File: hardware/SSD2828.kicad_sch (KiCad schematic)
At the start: 61 parts, among them IC1 TLV62568DBVR, J1 FH35C-25S-0.3SHW_50_, J3 Conn_01x34, U1 PAM2306DYPAA, U2 SSD2828QN4, Y1 24mhz

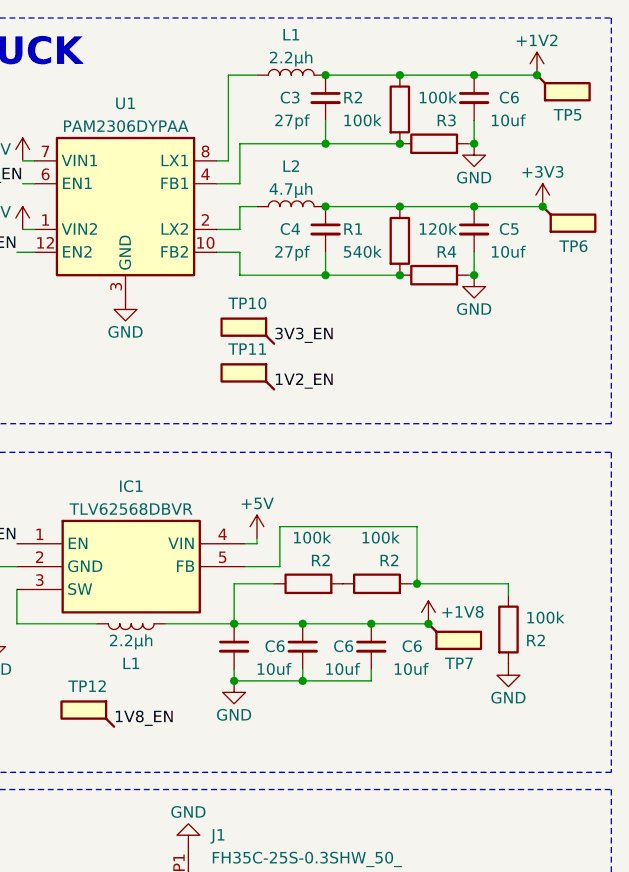
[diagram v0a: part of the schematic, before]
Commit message: added solder bridges on all the generated voltage rails on the SSD2828 board
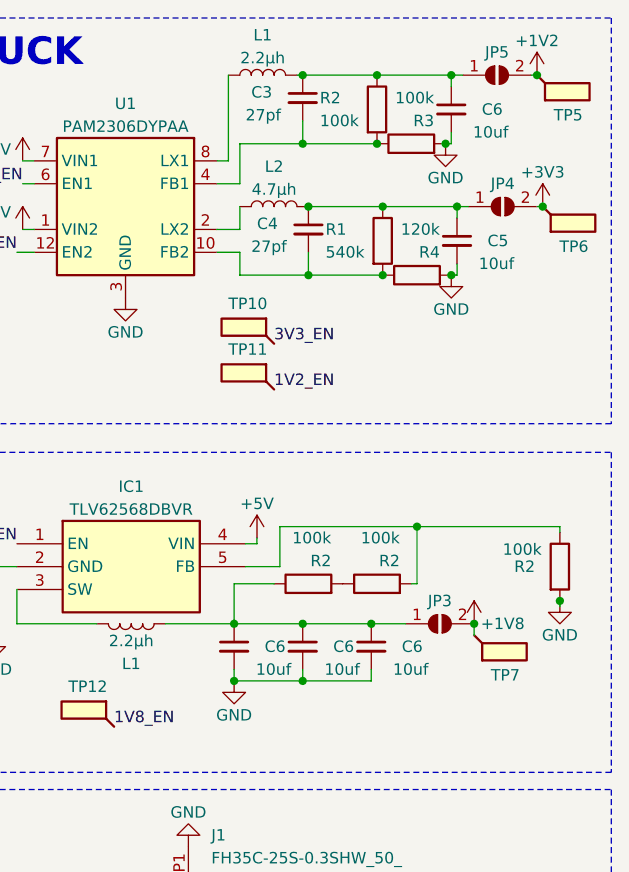
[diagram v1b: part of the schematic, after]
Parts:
- added JP3, JP4, JP5: SolderJumper_2_Open, Jumper:SolderJumper-2_P1.3mm_Open_Pad1.0x1.5mm, symbol Jumper:SolderJumper_2_Open
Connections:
- net +1V2: now also JP5.2 (B); no longer C3.1, C6.1, L1.2, R2.1
- net +1V8: now also JP3.2 (B); no longer C6.1, C6.1, C6.1, L1.2, R2.1
- net +3V3: now also JP4.2 (B); no longer C4.1, C5.1, L2.2, R1.1
- new net: C3.1, C6.1, JP5.1 (A), L1.2, R2.1
- new net: C6.1, C6.1, C6.1, JP3.1 (A), L1.2, R2.1
- new net: C4.1, C5.1, JP4.1 (A), L2.2, R1.1
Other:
- moved on the sheet: C3, C4, C5, C6, L1, L2, R1, R2, R3, R4, TP7

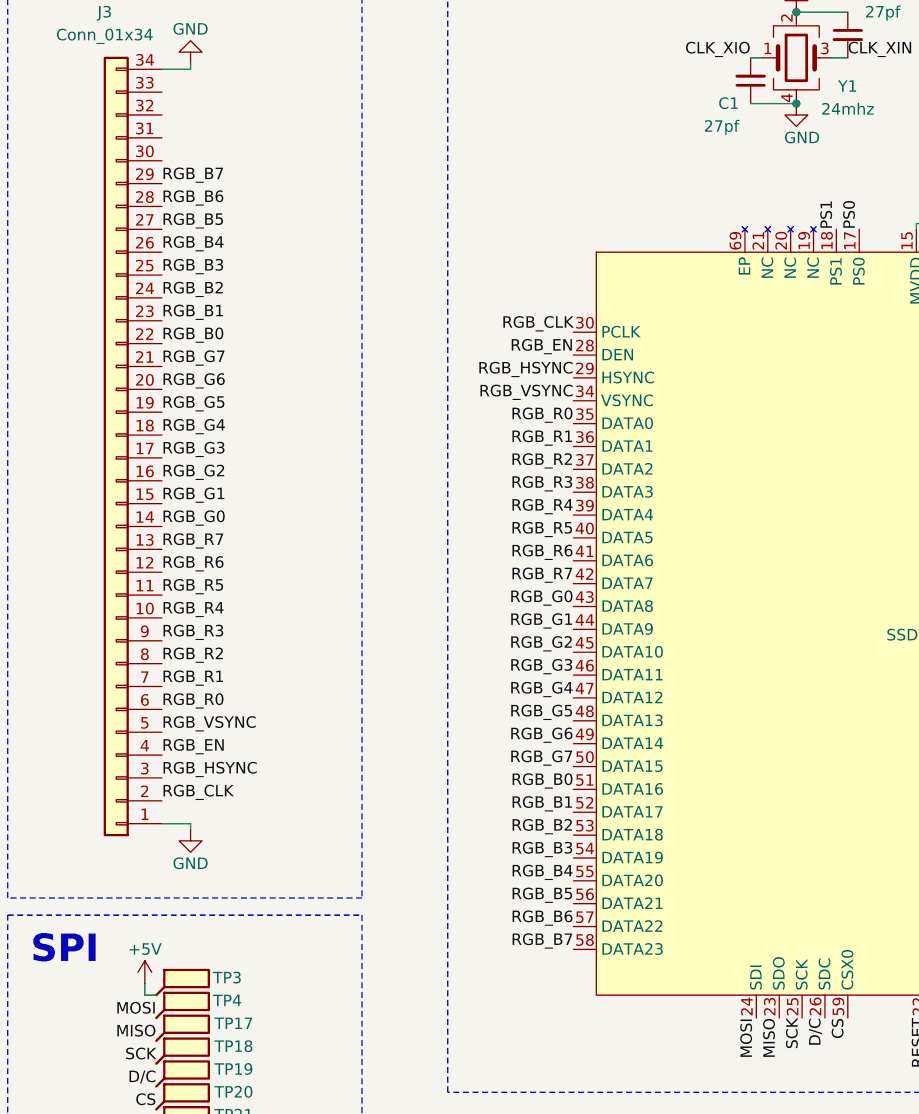
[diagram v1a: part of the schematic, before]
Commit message: changed the order of pins on the rgb connector + removed a pin from the schematic symbol
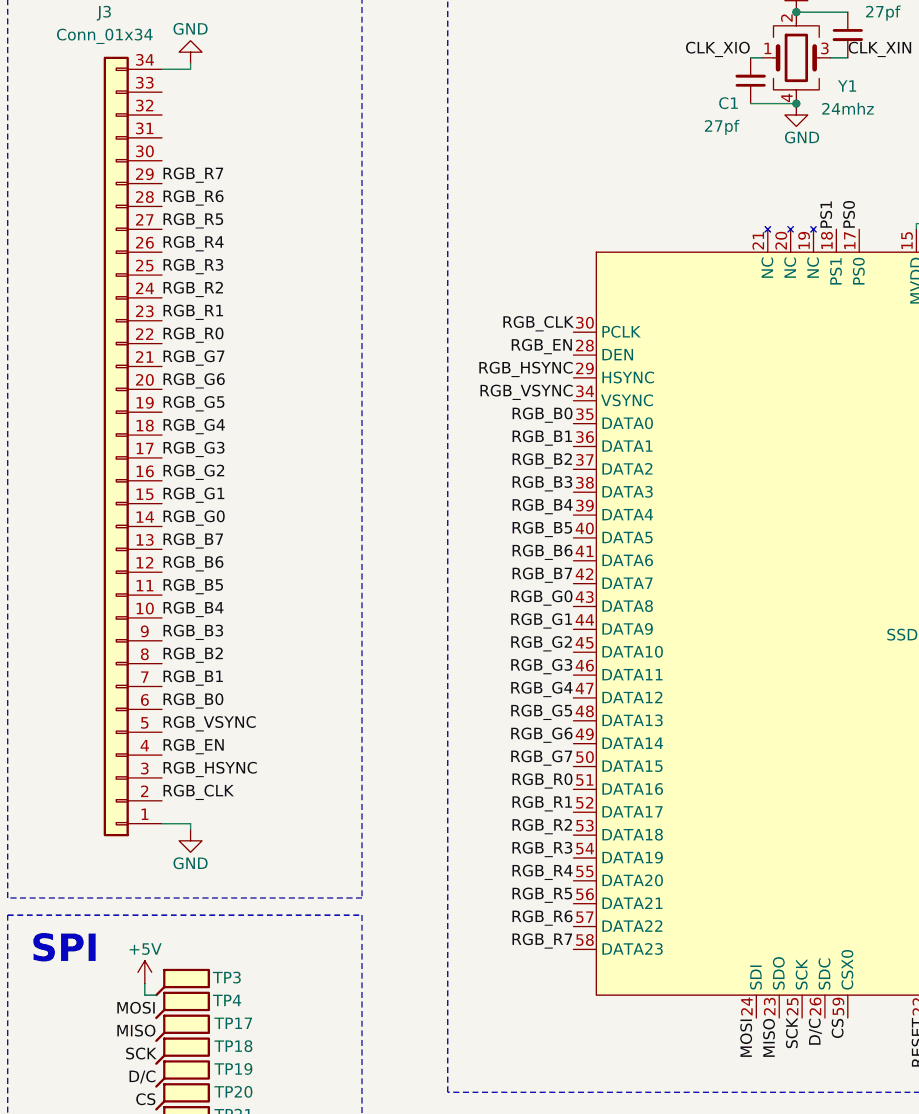
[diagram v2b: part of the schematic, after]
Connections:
- net RGB_B0: now also J3.6 (Pin_6), U2.35 (DATA0); no longer J3.22 (Pin_22), U2.51 (DATA16)
- net RGB_B1: now also J3.7 (Pin_7), U2.36 (DATA1); no longer J3.23 (Pin_23), U2.52 (DATA17)
- net RGB_B2: now also J3.8 (Pin_8), U2.37 (DATA2); no longer J3.24 (Pin_24), U2.53 (DATA18)
- net RGB_B3: now also J3.9 (Pin_9), U2.38 (DATA3); no longer J3.25 (Pin_25), U2.54 (DATA19)
- net RGB_B4: now also J3.10 (Pin_10), U2.39 (DATA4); no longer J3.26 (Pin_26), U2.55 (DATA20)
- net RGB_B5: now also J3.11 (Pin_11), U2.40 (DATA5); no longer J3.27 (Pin_27), U2.56 (DATA21)
- net RGB_B6: now also J3.12 (Pin_12), U2.41 (DATA6); no longer J3.28 (Pin_28), U2.57 (DATA22)
- net RGB_B7: now also J3.13 (Pin_13), U2.42 (DATA7); no longer J3.29 (Pin_29), U2.58 (DATA23)
- net RGB_R0: now also J3.22 (Pin_22), U2.51 (DATA16); no longer J3.6 (Pin_6), U2.35 (DATA0)
- net RGB_R1: now also J3.23 (Pin_23), U2.52 (DATA17); no longer J3.7 (Pin_7), U2.36 (DATA1)
- net RGB_R2: now also J3.24 (Pin_24), U2.53 (DATA18); no longer J3.8 (Pin_8), U2.37 (DATA2)
- net RGB_R3: now also J3.25 (Pin_25), U2.54 (DATA19); no longer J3.9 (Pin_9), U2.38 (DATA3)
- net RGB_R4: now also J3.26 (Pin_26), U2.55 (DATA20); no longer J3.10 (Pin_10), U2.39 (DATA4)
- net RGB_R5: now also J3.27 (Pin_27), U2.56 (DATA21); no longer J3.11 (Pin_11), U2.40 (DATA5)
- net RGB_R6: now also J3.28 (Pin_28), U2.57 (DATA22); no longer J3.12 (Pin_12), U2.41 (DATA6)
- net RGB_R7: now also J3.29 (Pin_29), U2.58 (DATA23); no longer J3.13 (Pin_13), U2.42 (DATA7)
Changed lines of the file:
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@@
     (effects (font (size 1.27 1.27)) (justify right bottom))
   )
-  (label "RGB_R3" (at 77.47 78.105 180) (fields_autoplaced)
+  (label "RGB_R3" (at 77.47 118.745 180) (fields_autoplaced)
     (effects (font (size 1.27 1.27)) (justify right bottom))
   )
@@
     (effects (font (size 1.27 1.27)) (justify right bottom))
   )
-  (label "RGB_B5" (at 77.47 123.825 180) (fields_autoplaced)
+  (label "RGB_B5" (at 77.47 83.185 180) (fields_autoplaced)
     (effects (font (size 1.27 1.27)) (justify right bottom))
   )
@@
     (effects (font (size 1.27 1.27)) (justify left bottom))
   )
-  (label "RGB_R6" (at 77.47 85.725 180) (fields_autoplaced)
+  (label "RGB_R6" (at 77.47 126.365 180) (fields_autoplaced)
     (effects (font (size 1.27 1.27)) (justify right bottom))
   )
@@
     (effects (font (size 1.27 1.27)) (justify right bottom))
   )
-  (label "RGB_B7" (at 31.75 43.815 0) (fields_autoplaced)
+  (label "RGB_B7" (at 31.75 84.455 0) (fields_autoplaced)
     (effects (font (size 1.27 1.27)) (justify left bottom))
   )
@@
     (effects (font (size 1.27 1.27)) (justify right bottom))
   )
-  (label "RGB_R2" (at 31.75 97.155 0) (fields_autoplaced)
+  (label "RGB_R2" (at 31.75 56.515 0) (fields_autoplaced)
     (effects (font (size 1.27 1.27)) (justify left bottom))
   )
@@
     (effects (font (size 1.27 1.27)) (justify right bottom))
   )
-  (label "RGB_R0" (at 77.47 70.485 180) (fields_autoplaced)
+  (label "RGB_R0" (at 77.47 111.125 180) (fields_autoplaced)
     (effects (font (size 1.27 1.27)) (justify right bottom))
   )
-  (label "RGB_B3" (at 77.47 118.745 180) (fields_autoplaced)
+  (label "RGB_B3" (at 77.47 78.105 180) (fields_autoplaced)
     (effects (font (size 1.27 1.27)) (justify right bottom))
   )
@@
     (effects (font (size 1.27 1.27)) (justify left bottom))
   )
-  (label "RGB_R5" (at 31.75 89.535 0) (fields_autoplaced)
+  (label "RGB_R5" (at 31.75 48.895 0) (fields_autoplaced)
     (effects (font (size 1.27 1.27)) (justify left bottom))
   )
@@
     (effects (font (size 1.27 1.27)) (justify left bottom))
   )
-  (label "RGB_R4" (at 77.47 80.645 180) (fields_autoplaced)
+  (label "RGB_R4" (at 77.47 121.285 180) (fields_autoplaced)
     (effects (font (size 1.27 1.27)) (justify right bottom))
   )
@@
     (effects (font (size 1.27 1.27)) (justify left bottom))
   )
-  (label "RGB_B2" (at 77.47 116.205 180) (fields_autoplaced)
+  (label "RGB_B2" (at 77.47 75.565 180) (fields_autoplaced)
     (effects (font (size 1.27 1.27)) (justify right bottom))
   )
@@
     (effects (font (size 1.27 1.27)) (justify right bottom))
   )
-  (label "RGB_B4" (at 31.75 51.435 0) (fields_autoplaced)
+  (label "RGB_B4" (at 31.75 92.075 0) (fields_autoplaced)
     (effects (font (size 1.27 1.27)) (justify left bottom))
   )
-  (label "RGB_B0" (at 77.47 111.125 180) (fields_autoplaced)
+  (label "RGB_B0" (at 77.47 70.485 180) (fields_autoplaced)
     (effects (font (size 1.27 1.27)) (justify right bottom))
   )
-  (label "RGB_R7" (at 77.47 88.265 180) (fields_autoplaced)
+  (label "RGB_R7" (at 77.47 128.905 180) (fields_autoplaced)
     (effects (font (size 1.27 1.27)) (justify right bottom))
   )
@@
     (effects (font (size 1.27 1.27)) (justify right bottom))
   )
-  (label "RGB_B3" (at 31.75 53.975 0) (fields_autoplaced)
+  (label "RGB_B3" (at 31.75 94.615 0) (fields_autoplaced)
     (effects (font (size 1.27 1.27)) (justify left bottom))
   )
-  (label "RGB_B1" (at 77.47 113.665 180) (fields_autoplaced)
+  (label "RGB_B1" (at 77.47 73.025 180) (fields_autoplaced)
     (effects (font (size 1.27 1.27)) (justify right bottom))
   )
@@
     (effects (font (size 1.27 1.27)) (justify left bottom))
   )
-  (label "RGB_R7" (at 31.75 84.455 0) (fields_autoplaced)
+  (label "RGB_R7" (at 31.75 43.815 0) (fields_autoplaced)
     (effects (font (size 1.27 1.27)) (justify left bottom))
   )
@@
     (effects (font (size 1.27 1.27)) (justify right bottom))
   )
-  (label "RGB_R3" (at 31.75 94.615 0) (fields_autoplaced)
+  (label "RGB_R3" (at 31.75 53.975 0) (fields_autoplaced)
     (effects (font (size 1.27 1.27)) (justify left bottom))
   )
@@
     (effects (font (size 1.27 1.27)) (justify left bottom))
   )
-  (label "RGB_B4" (at 77.47 121.285 180) (fields_autoplaced)
+  (label "RGB_B4" (at 77.47 80.645 180) (fields_autoplaced)
     (effects (font (size 1.27 1.27)) (justify right bottom))
   )
@@
     (effects (font (size 1.27 1.27)) (justify left bottom))
   )
-  (label "RGB_B6" (at 31.75 46.355 0) (fields_autoplaced)
+  (label "RGB_B6" (at 31.75 86.995 0) (fields_autoplaced)
     (effects (font (size 1.27 1.27)) (justify left bottom))
   )
-  (label "RGB_R5" (at 77.47 83.185 180) (fields_autoplaced)
+  (label "RGB_R5" (at 77.47 123.825 180) (fields_autoplaced)
     (effects (font (size 1.27 1.27)) (justify right bottom))
   )
@@
     (effects (font (size 1.27 1.27)) (justify right bottom))
   )
-  (label "RGB_R6" (at 31.75 86.995 0) (fields_autoplaced)
+  (label "RGB_R6" (at 31.75 46.355 0) (fields_autoplaced)
     (effects (font (size 1.27 1.27)) (justify left bottom))
   )
@@
     (effects (font (size 1.27 1.27)) (justify left bottom))
   )
-  (label "RGB_B7" (at 77.47 128.905 180) (fields_autoplaced)
+  (label "RGB_B7" (at 77.47 88.265 180) (fields_autoplaced)
     (effects (font (size 1.27 1.27)) (justify right bottom))
   )
@@
     (effects (font (size 1.27 1.27)) (justify right bottom))
   )
-  (label "RGB_B6" (at 77.47 126.365 180) (fields_autoplaced)
+  (label "RGB_B6" (at 77.47 85.725 180) (fields_autoplaced)
     (effects (font (size 1.27 1.27)) (justify right bottom))
   )
-  (label "RGB_R1" (at 31.75 99.695 0) (fields_autoplaced)
+  (label "RGB_R1" (at 31.75 59.055 0) (fields_autoplaced)
     (effects (font (size 1.27 1.27)) (justify left bottom))
   )
@@
     (effects (font (size 1.27 1.27)) (justify left bottom))
   )
-  (label "RGB_B0" (at 31.75 61.595 0) (fields_autoplaced)
+  (label "RGB_B0" (at 31.75 102.235 0) (fields_autoplaced)
     (effects (font (size 1.27 1.27)) (justify left bottom))
   )
@@
     (effects (font (size 1.27 1.27)) (justify right bottom))
   )
-  (label "RGB_B2" (at 31.75 56.515 0) (fields_autoplaced)
+  (label "RGB_B2" (at 31.75 97.155 0) (fields_autoplaced)
     (effects (font (size 1.27 1.27)) (justify left bottom))
   )
@@
     (effects (font (size 1.27 1.27)) (justify right bottom))
   )
-  (label "RGB_R4" (at 31.75 92.075 0) (fields_autoplaced)
+  (label "RGB_R4" (at 31.75 51.435 0) (fields_autoplaced)
     (effects (font (size 1.27 1.27)) (justify left bottom))
   )
-  (label "RGB_B1" (at 31.75 59.055 0) (fields_autoplaced)
+  (label "RGB_B1" (at 31.75 99.695 0) (fields_autoplaced)
     (effects (font (size 1.27 1.27)) (justify left bottom))
   )
@@
     (effects (font (size 1.27 1.27)) (justify right bottom))
   )
-  (label "RGB_R1" (at 77.47 73.025 180) (fields_autoplaced)
+  (label "RGB_R1" (at 77.47 113.665 180) (fields_autoplaced)
     (effects (font (size 1.27 1.27)) (justify right bottom))
   )
-  (label "RGB_B5" (at 31.75 48.895 0) (fields_autoplaced)
+  (label "RGB_B5" (at 31.75 89.535 0) (fields_autoplaced)
     (effects (font (size 1.27 1.27)) (justify left bottom))
   )
-  (label "RGB_R0" (at 31.75 102.235 0) (fields_autoplaced)
+  (label "RGB_R0" (at 31.75 61.595 0) (fields_autoplaced)
     (effects (font (size 1.27 1.27)) (justify left bottom))
   )
-  (label "RGB_R2" (at 77.47 75.565 180) (fields_autoplaced)
+  (label "RGB_R2" (at 77.47 116.205 180) (fields_autoplaced)
     (effects (font (size 1.27 1.27)) (justify right bottom))
   )
@@
     (pin "68")
     (pin "69")
-    (pin "69")
     (pin "7")

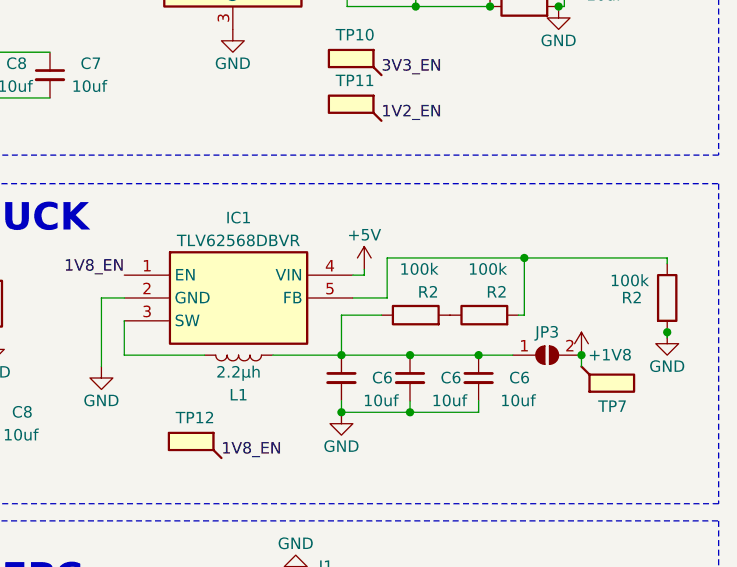
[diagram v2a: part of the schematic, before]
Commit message: retouched copper fills + started reordering the power nets
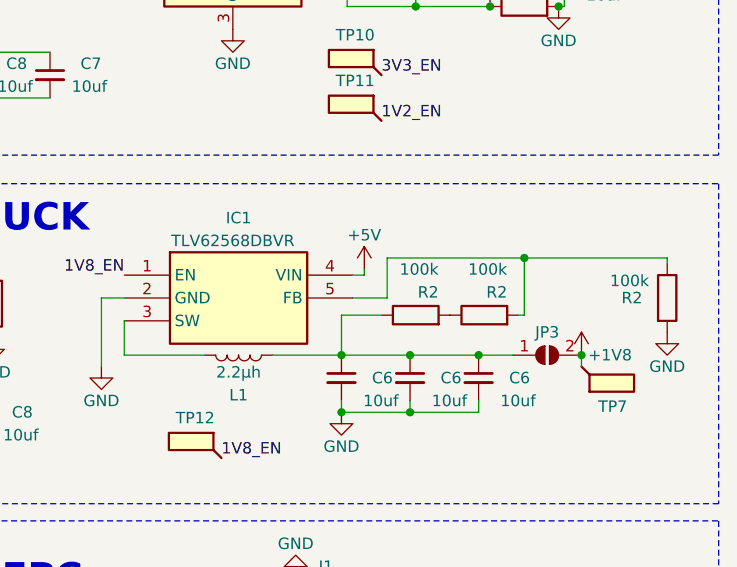
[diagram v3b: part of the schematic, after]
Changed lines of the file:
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@@
   (junction (at 127 26.035) (diameter 0) (color 0 0 0 0)
   )
-  (junction (at 276.225 79.375) (diameter 0) (color 0 0 0 0)
-  )
   (junction (at 199.39 53.34) (diameter 0) (color 0 0 0 0)
   )
@@
   )
   (wire (pts (xy 31.75 114.935) (xy 34.925 114.935))
-    (stroke (width 0) (type default))
-  )
-  (wire (pts (xy 276.225 79.375) (xy 276.225 80.01))
     (stroke (width 0) (type default))
   )
@@
   )
   (symbol (lib_id "SamacSys_Parts:TLV62568DBVR") (at 215.9 73.025 0) (unit 1)
-    (in_bom yes) (on_board yes) (dnp no) (fields_autoplaced)
+    (in_bom yes) (on_board yes) (dnp no)
     (property "Reference" "IC1" (at 228.6 66.675 0)
       (effects (font (size 1.27 1.27)))
     )
-    (property "Value" "TLV62568DBVR" (at 228.6 69.215 0)
-      (effects (font (size 1.27 1.27)))
-    )
+    (property "Value" "TLV62568DBVR" (at 227.965 69.215 0)
+      (effects (font (size 1.27 1.27)))
+    )
